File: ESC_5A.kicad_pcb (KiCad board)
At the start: 2 copper layers, 39 parts, among them IC1 EEPROM, IC2 3.3V Reg, IC3 5V_Reg, IC4 ATSAMD21E17D-AUT, J1 USBc, J2 5V_PWR, J3 M1, J4 M2, J5 PWR_IN, U1 TB67H420FTG_EL

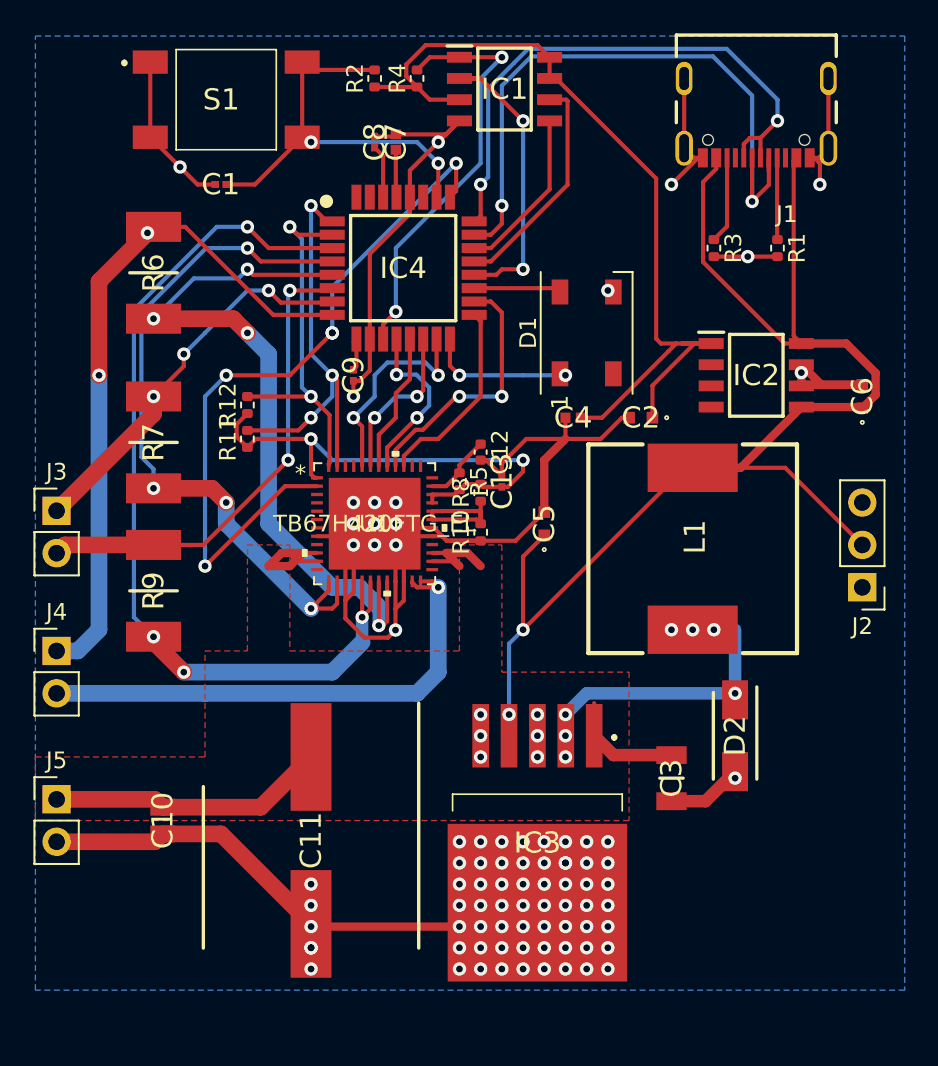
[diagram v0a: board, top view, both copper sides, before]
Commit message: Smaller board Created but fears of the issues with GND connections
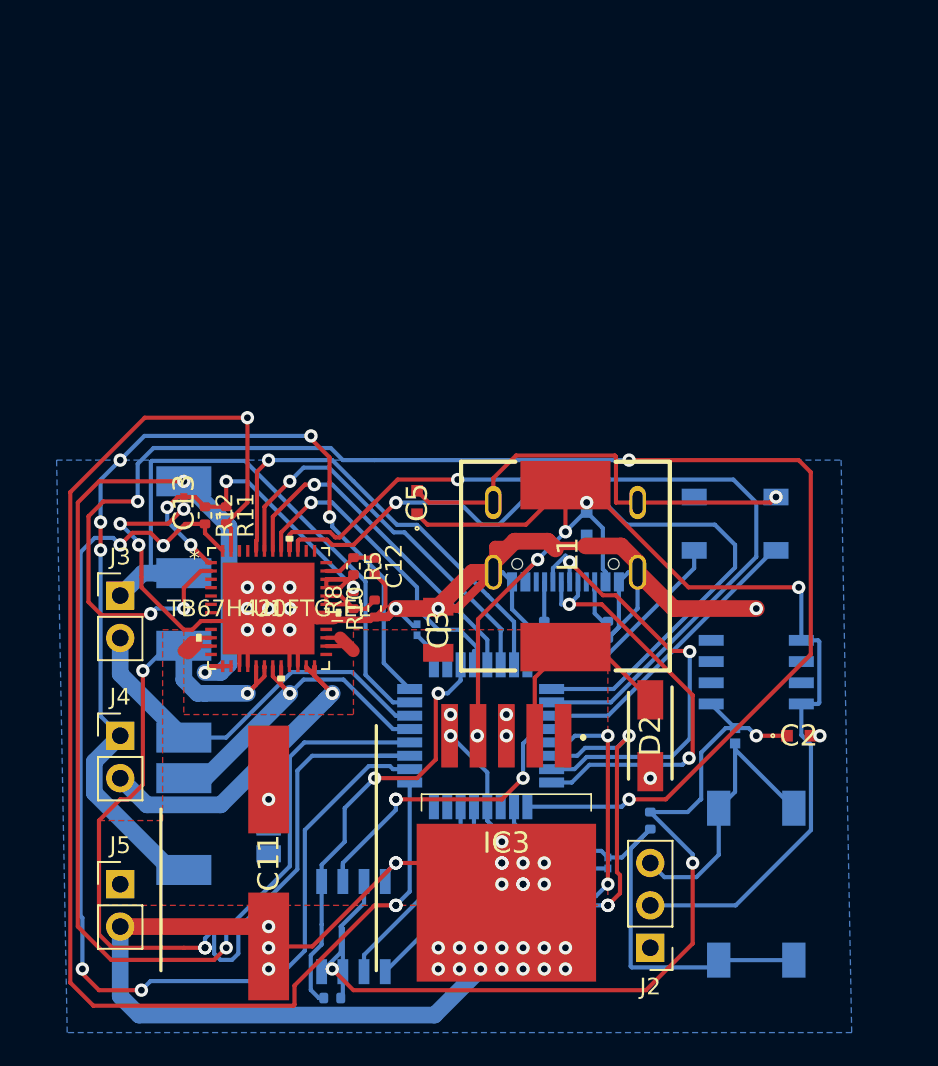
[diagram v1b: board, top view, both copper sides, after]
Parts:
- C1, C10, C4, C6, C7, C8, C9, D1, IC1, IC2, IC4, J1, R1, R2, R3, R4, R6, R7, R9, S1: moved to B.Cu
- moved S1 56.7 mm to (194.3, 44.5), turned to 270 degrees
- moved R4 55.3 mm to (168.9, 51.3), turned to 180 degrees
- moved IC1 51.0 mm to (170.2, 47.0), turned to 270 degrees
- moved R2 47.4 mm to (188.0, 40.6), turned to 270 degrees
- moved C1 46.8 mm to (185.4, 43.2), turned to 90 degrees
- moved C7 42.2 mm to (177.8, 41.9), turned to 270 degrees
- moved C8 42.2 mm to (176.5, 41.9), turned to 90 degrees
- moved R6 33.1 mm to (160.0, 40.9), turned to 270 degrees
- moved IC4 28.4 mm to (177.8, 35.6)
- moved J1 27.9 mm to (182.9, 21.6), turned to 0 degrees
- moved R1 26.8 mm to (181.6, 29.2)
- moved J2 25.0 mm to (188.0, 48.3)
- moved R3 23.7 mm to (185.4, 29.2)
- moved C4 21.4 mm to (193.0, 35.6), turned to 270 degrees
- moved C2 21.3 mm to (196.8, 35.6), turned to 0 degrees
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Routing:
- net LO1: track 25.1 -> 81.4 mm
- net GND: track 171.6 -> 225.4 mm, vias 88 -> 50
- net HBMODE: track 43.5 -> 93.8 mm
- net LO2: track 21.9 -> 66.8 mm, vias 2 -> 4
- net PWMB: track 15.8 -> 52.6 mm, vias 2 -> 1
- net ADC_VREFA: track 42.4 -> 79.0 mm, vias 4 -> 3
- net PWMA: track 11.7 -> 46.1 mm, vias 0 -> 1
- net ADC_VREFB: track 48.5 -> 21.1 mm, vias 4 -> 1
- net PWR_IN: track 37.8 -> 12.1 mm, vias 0 -> 1
- net MOSI_EEPROM: track 10.1 -> 31.0 mm, vias 0 -> 3
- net ADC_2: track 41.4 -> 58.5 mm, vias 2 -> 5
- net SCK_EEPROM: track 13.6 -> 29.8 mm, vias 0 -> 2
- net INB2: track 12.8 -> 27.6 mm, vias 2 -> 1
- net INB1: track 9.66 -> 24.0 mm, vias 2 -> 1
- net INA2: track 8.38 -> 21.0 mm, vias 0 -> 1
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
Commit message: feather profile
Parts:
- C1, C10, C4, C6, C7, C8, C9, D1, R1, R2, R3, R4, S1: moved to F.Cu
- C11: footprint SamacSys_Parts:CAPAE1290X1650N -> SamacSys_Parts:CAPAE660X800N
- D2: moved to B.Cu
- L1: footprint SamacSys_Parts:SRR1260-150M -> SamacSys_Parts:INDM8680X300N
- moved J1 102.6 mm to (278.1, 59.7), turned to 270 degrees
- moved IC1 94.3 mm to (264.2, 54.6), turned to 0 degrees
- moved L1 88.0 mm to (261.6, 64.8), turned to 0 degrees
- moved D1 87.6 mm to (275.6, 52.1)
- moved J4 86.3 mm to (236.2, 67.9), turned to 90 degrees
- moved J2 86.0 mm to (271.8, 67.3), turned to 90 degrees
- moved C9 84.7 mm to (257.7, 41.9), turned to 0 degrees
- moved J3 84.2 mm to (229.9, 67.9), turned to 90 degrees
- moved R6 79.2 mm to (236.3, 62.2)
- moved R7 78.9 mm to (228.6, 62.2)
- moved C8 78.8 mm to (255.3, 43.7), turned to 0 degrees
- moved R9 78.1 mm to (232.4, 62.2)
- moved R4 77.9 mm to (246.4, 43.2), turned to 0 degrees
- moved C7 77.8 mm to (255.5, 38.1), turned to 0 degrees
- moved IC4 75.9 mm to (250.2, 58.4)
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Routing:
- net GND: track 225.4 -> 70.8 mm, vias 50 -> 7
- net HBMODE: track 93.8 -> 0.00 mm, vias 5 -> 0
- net LO1: track 81.4 -> 3.35 mm, vias 3 -> 0
- net ADC_VREFA: track 79.0 -> 7.06 mm, vias 3 -> 1
- net LO2: track 66.8 -> 1.97 mm, vias 4 -> 0
- net +5V: track 81.4 -> 17.2 mm, vias 5 -> 0
- net +3V3: track 58.6 -> 0.00 mm, vias 3 -> 0
- net PWMB: track 52.6 -> 0.00 mm, vias 1 -> 0
- net PWMA: track 46.1 -> 0.00 mm, vias 1 -> 0
- net ADC_2: track 58.5 -> 25.3 mm, vias 5 -> 0
- net MOSI_EEPROM: track 31.0 -> 0.00 mm, vias 3 -> 0
- net SCK_EEPROM: track 29.8 -> 0.00 mm, vias 2 -> 0
- net NRST: track 29.4 -> 0.00 mm
- net D-: track 27.6 -> 0.00 mm, vias 2 -> 0
- net INB2: track 27.6 -> 0.00 mm, vias 1 -> 0
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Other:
- board outline added: 62.2 x 24.1 mm

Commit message: Remote work
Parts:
- C1, C3, C4, C7, C8, C9, R1, R3: moved to B.Cu
- moved C6 37.6 mm to (252.7, 73.7)
- moved C5 35.6 mm to (256.5, 73.7)
- moved C3 30.5 mm to (242.6, 67.3), turned to 90 degrees
- moved R3 29.3 mm to (270.5, 61.0), turned to 180 degrees
- moved R1 28.9 mm to (270.5, 58.4), turned to 180 degrees
- moved C7 28.7 mm to (248.9, 66.0), turned to 270 degrees
- moved C8 23.6 mm to (247.7, 66.0), turned to 90 degrees
- moved C9 15.2 mm to (246.4, 52.1), turned to 270 degrees
- moved C4 11.3 mm to (259.1, 50.8)
- moved C1 8.52 mm to (259.1, 49.5)
- moved IC1 2.54 mm to (264.2, 52.1)
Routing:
- net LO1: track 3.35 -> 65.8 mm, vias 0 -> 1
- net HBMODE: track 0.00 -> 61.8 mm, vias 0 -> 1
- net LO2: track 1.97 -> 60.7 mm, vias 0 -> 1
- net +5V: track 17.2 -> 54.6 mm, vias 0 -> 1
- net ADC_VREFA: track 7.06 -> 41.9 mm, vias 1 -> 3
- net GND: track 70.8 -> 98.9 mm, vias 7 -> 17
- net PWR_IN: track 13.4 -> 40.9 mm, vias 0 -> 1
- net D-: track 0.00 -> 27.3 mm, vias 0 -> 2
- net D+: track 0.00 -> 25.2 mm, vias 0 -> 2
- net +3V3: track 0.00 -> 21.0 mm, vias 0 -> 2
- net MOSI_EEPROM: track 0.00 -> 19.1 mm, vias 0 -> 2
- net ADC_VREFB: track 7.98 -> 26.1 mm
- net SCK_EEPROM: track 0.00 -> 15.5 mm
- net MISO_EEPROM: track 0.00 -> 9.22 mm
- net Net-(C8-Pad2): track 0.00 -> 3.60 mm
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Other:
- board size 62.2 x 24.1 mm -> 62.2 x 25.4 mm
